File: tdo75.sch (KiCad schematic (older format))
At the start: 15 parts

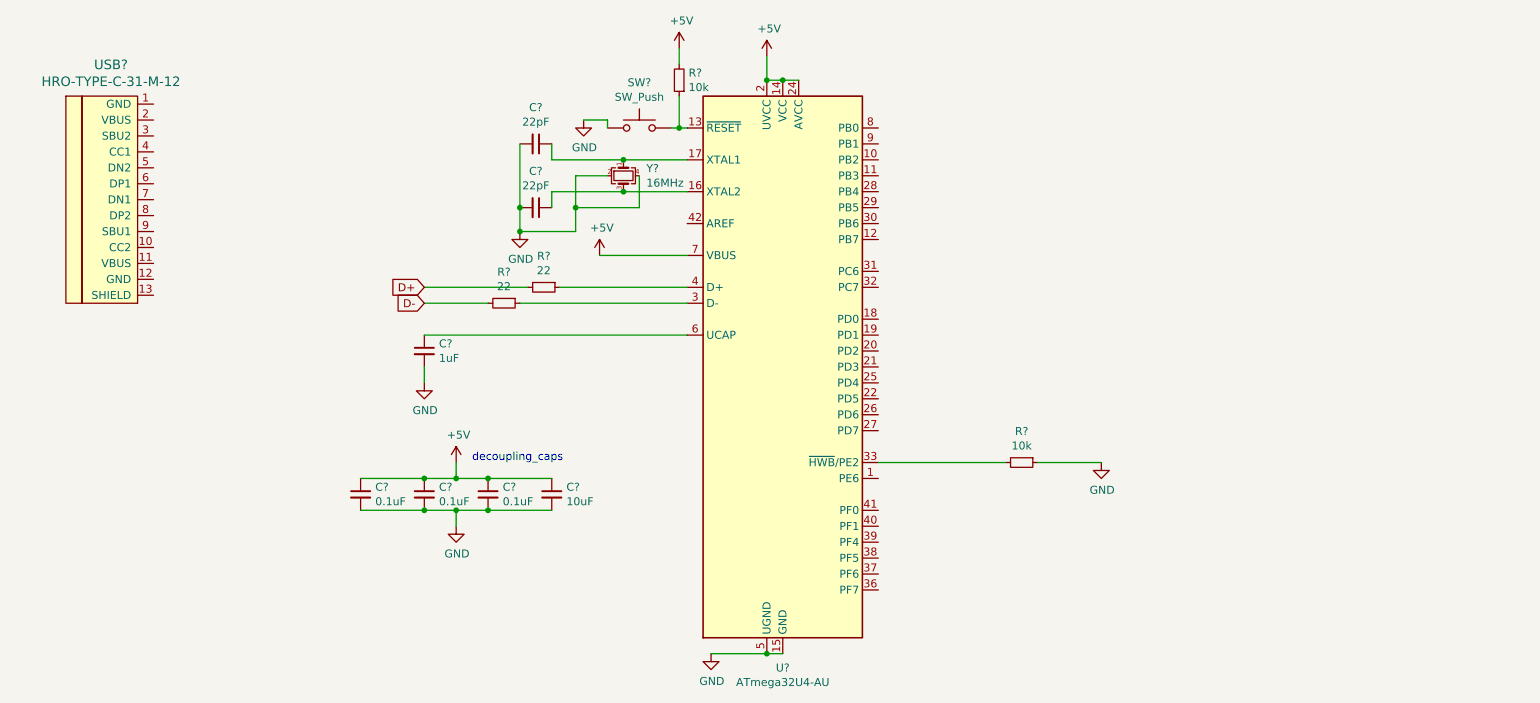
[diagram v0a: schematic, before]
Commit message: map footprints to schematics
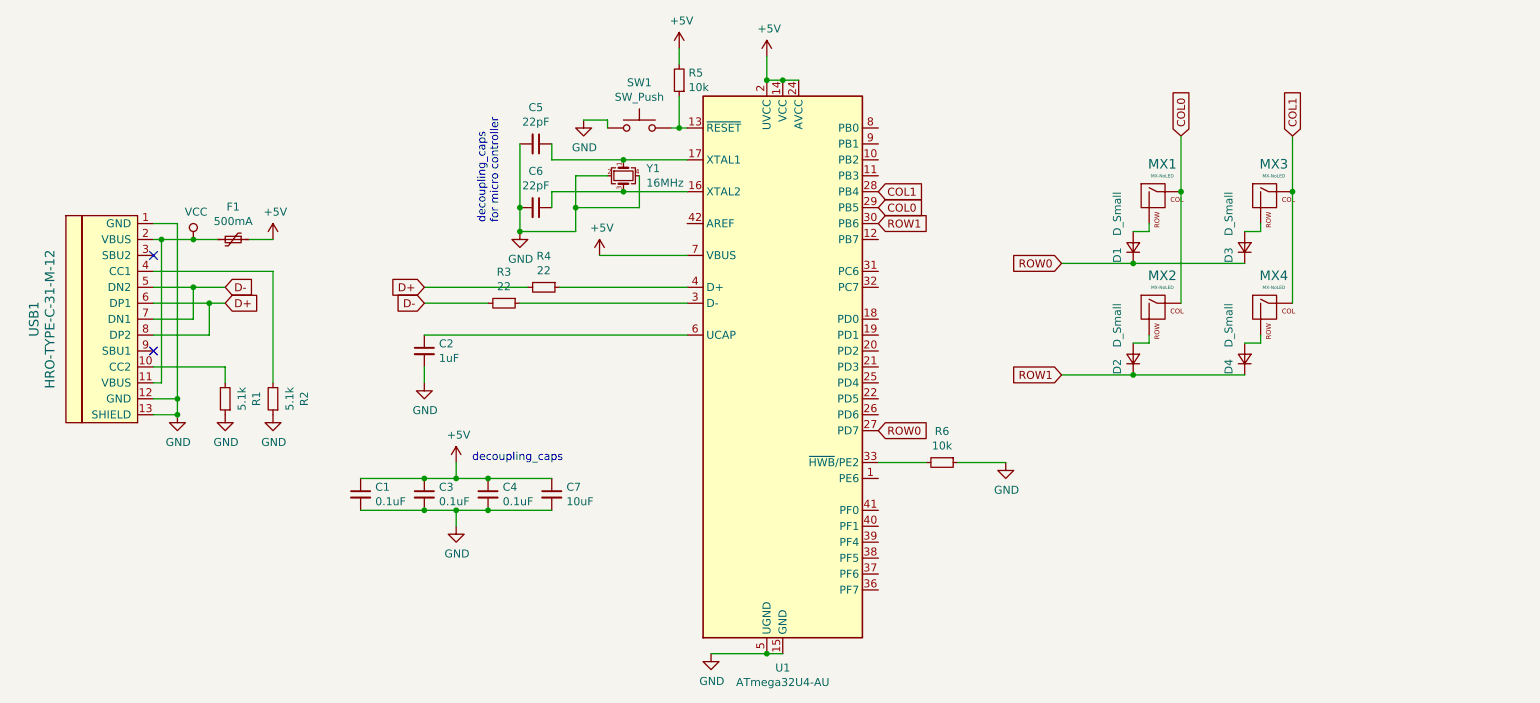
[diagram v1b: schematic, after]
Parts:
- added D1, D2, D3, D4: D_Small, Diode_SMD:D_SOD-123, symbol Device:D_Small
- added F1: 500mA, Fuse:Fuse_1206_3216Metric, symbol Device:Polyfuse_Small
- added MX1, MX2, MX3, MX4: MX-NoLED, MX_Only:MXOnly-1U-NoLED, symbol MX_Alps_Hybrid:MX-NoLED
- added R1, R2: 5.1k, Resistor_SMD:R_0805_2012Metric, symbol Device:R_Small
- C1, C2, C3, C4, C5, C6, C7: renamed from C?; footprint (none) -> Capacitor_SMD:C_0805_2012Metric
- R3, R4, R5, R6: renamed from R?; footprint (none) -> Resistor_SMD:R_0805_2012Metric
- SW1: renamed from SW?; footprint (none) -> random-keyboard-parts:SKQG-1155865
- USB1: renamed from USB?; footprint (none) -> Type-C:HRO-TYPE-C-31-M-12
- Y1: renamed from Y?; footprint (none) -> Crystal:Crystal_SMD_3225-4Pin_3.2x2.5mm
- gave numbers to parts that had none: 1
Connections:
- net +5V: now also F1.1
- net D+: now also USB1.6 (DP1), USB1.8 (DP2)
- net D-: now also USB1.5 (DN2), USB1.7 (DN1)
- net GND: now also USB1.1 (GND), USB1.12 (GND), USB1.13 (SHIELD), R1.1, R2.1
- net ROW0: now reaches U1.27 (PD7)
- net ROW0: now also D1.1 (K), D3.1 (K)
- net COL1: now reaches U1.28 (PB4)
- net COL1: now also MX3.1 (COL), MX4.1 (COL)
- net COL0: now reaches U1.29 (PB5)
- net COL0: now also MX1.1 (COL), MX2.1 (COL)
- net ROW1: now reaches U1.30 (PB6)
- net ROW1: now also D2.1 (K), D4.1 (K)
- net at USB1.10 (CC2): now also R1.2
- net VCC: now reaches USB1.11 (VBUS)
- net VCC: now also USB1.2 (VBUS), F1.2
- net at USB1.4 (CC1): now also R2.2
- new net: D1.2 (A), MX1.2 (ROW)
- new net: D2.2 (A), MX2.2 (ROW)
- new net: D4.2 (A), MX4.2 (ROW)
- new net: D3.2 (A), MX3.2 (ROW)
- no-connect marks 0 -> 2
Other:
- note added: "decoupling_caps \nfor micro controller\n\n"
- moved on the sheet: R6, USB1

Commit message: heirarchical keyboard matrix
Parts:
- removed D1, D2, D3, D4: D_Small, Diode_SMD:D_SOD-123, symbol Device:D_Small
- removed MX1, MX2, MX3, MX4: MX-NoLED, MX_Only:MXOnly-1U-NoLED, symbol MX_Alps_Hybrid:MX-NoLED
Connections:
- net COL0: now also U1.8 (PB0); no longer U1.29 (PB5)
- net COL1: now also U1.9 (PB1); no longer U1.28 (PB4)
- net ROW0: now also U1.41 (PF0); no longer U1.27 (PD7)
- net ROW1: now also U1.40 (PF1); no longer U1.30 (PB6)
- net COL2: now reaches U1.10 (PB2)
- net COL3: now reaches U1.11 (PB3)
- net COL7: now reaches U1.12 (PB7)
- net COL8: now reaches U1.18 (PD0)
- net COL9: now reaches U1.19 (PD1)
- net COL10: now reaches U1.20 (PD2)
- net COL11: now reaches U1.21 (PD3)
- net COL13: now reaches U1.22 (PD5)
- net COL12: now reaches U1.25 (PD4)
- net COL14: now reaches U1.26 (PD6)
- net ROW4: now reaches U1.37 (PF6)
- net ROW3: now reaches U1.38 (PF5)
- net ROW2: now reaches U1.39 (PF4)
- new net COL15: U1.27 (PD7)
- new net COL4: U1.28 (PB4)
- new net COL5: U1.29 (PB5)
- new net COL6: U1.30 (PB6)
- no-connect marks 2 -> 6
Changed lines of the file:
@@
 $Descr A4 11693 8268
 encoding utf-8
-Sheet 1 1
+Sheet 1 2
 Title ""
 Date ""
@@
 NoConn ~ 1550 4100
 NoConn ~ 1550 3500
-$Comp
-L MX_Alps_Hybrid:MX-NoLED MX1
-U 1 1 5E7B02A9
-P 7850 3150
-F 0 "MX1" H 7883 3373 60  0000 C CNN
-F 1 "MX-NoLED" H 7883 3299 20  0000 C CNN
-F 2 "MX_Only:MXOnly-1U-NoLED" H 7225 3125 60  0001 C CNN
-F 3 "" H 7225 3125 60  0001 C CNN
-	1    7850 3150
-	1    0    0    -1
-$EndComp
-$Comp
-L MX_Alps_Hybrid:MX-NoLED MX2
-U 1 1 5E7B0859
-P 7850 3850
-F 0 "MX2" H 7883 4073 60  0000 C CNN
-F 1 "MX-NoLED" H 7883 3999 20  0000 C CNN
-F 2 "MX_Only:MXOnly-1U-NoLED" H 7225 3825 60  0001 C CNN
-F 3 "" H 7225 3825 60  0001 C CNN
-	1    7850 3850
-	1    0    0    -1
-$EndComp
-$Comp
-L MX_Alps_Hybrid:MX-NoLED MX4
-U 1 1 5E7B0B55
-P 8550 3850
-F 0 "MX4" H 8583 4073 60  0000 C CNN
-F 1 "MX-NoLED" H 8583 3999 20  0000 C CNN
-F 2 "MX_Only:MXOnly-1U-NoLED" H 7925 3825 60  0001 C CNN
-F 3 "" H 7925 3825 60  0001 C CNN
-	1    8550 3850
-	1    0    0    -1
-$EndComp
-$Comp
-L MX_Alps_Hybrid:MX-NoLED MX3
-U 1 1 5E7B0E66
-P 8550 3150
-F 0 "MX3" H 8583 3373 60  0000 C CNN
-F 1 "MX-NoLED" H 8583 3299 20  0000 C CNN
-F 2 "MX_Only:MXOnly-1U-NoLED" H 7925 3125 60  0001 C CNN
-F 3 "" H 7925 3125 60  0001 C CNN
-	1    8550 3150
-	1    0    0    -1
-$EndComp
-$Comp
-L Device:D_Small D1
-U 1 1 5E7B3897
-P 7700 3450
-F 0 "D1" H 7700 3550 50  0000 R CNN
-F 1 "D_Small" H 8050 3550 50  0000 R CNN
-F 2 "Diode_SMD:D_SOD-123" V 7700 3450 50  0001 C CNN
-F 3 "~" V 7700 3450 50  0001 C CNN
-	1    7700 3450
-	0    -1   -1   0
-$EndComp
-Wire Wire Line
-	7700 3350 7800 3350
-Wire Wire Line
-	7800 3350 7800 3300
-$Comp
-L Device:D_Small D2
-U 1 1 5E7B58A6
-P 7700 4150
-F 0 "D2" H 7700 4250 50  0000 R CNN
-F 1 "D_Small" H 8050 4250 50  0000 R CNN
-F 2 "Diode_SMD:D_SOD-123" V 7700 4150 50  0001 C CNN
-F 3 "~" V 7700 4150 50  0001 C CNN
-	1    7700 4150
-	0    -1   -1   0
-$EndComp
-$Comp
-L Device:D_Small D4
-U 1 1 5E7B5B76
-P 8400 4150
-F 0 "D4" H 8400 4250 50  0000 R CNN
-F 1 "D_Small" H 8750 4250 50  0000 R CNN
-F 2 "Diode_SMD:D_SOD-123" V 8400 4150 50  0001 C CNN
-F 3 "~" V 8400 4150 50  0001 C CNN
-	1    8400 4150
-	0    -1   -1   0
-$EndComp
-$Comp
-L Device:D_Small D3
-U 1 1 5E7B5E2E
-P 8400 3450
-F 0 "D3" H 8400 3550 50  0000 R CNN
-F 1 "D_Small" H 8750 3550 50  0000 R CNN
-F 2 "Diode_SMD:D_SOD-123" V 8400 3450 50  0001 C CNN
-F 3 "~" V 8400 3450 50  0001 C CNN
-	1    8400 3450
-	0    -1   -1   0
-$EndComp
-Wire Wire Line
-	7700 4050 7800 4050
-Wire Wire Line
-	7800 4050 7800 4000
-Wire Wire Line
-	8400 4050 8500 4050
-Wire Wire Line
-	8500 4050 8500 4000
-Wire Wire Line
-	8400 3350 8500 3350
-Wire Wire Line
-	8500 3350 8500 3300
-Wire Wire Line
-	8000 3800 8000 3100
-Wire Wire Line
-	8000 3100 8000 2750
-Connection ~ 8000 3100
-Wire Wire Line
-	8400 3550 7700 3550
-Wire Wire Line
-	7700 3550 7250 3550
-Connection ~ 7700 3550
-Wire Wire Line
-	8400 4250 7700 4250
-Wire Wire Line
-	7700 4250 7250 4250
-Connection ~ 7700 4250
-Wire Wire Line
-	8700 3800 8700 3100
-Wire Wire Line
-	8700 3100 8700 2750
-Connection ~ 8700 3100
-Text GLabel 8000 2750 1    50   Input ~ 0
+Text GLabel 6100 2800 2    50   Input ~ 0
+COL1
+Text GLabel 6100 2700 2    50   Input ~ 0
 COL0
-Text GLabel 8700 2750 1    50   Input ~ 0
-COL1
-Text GLabel 7250 4250 0    50   Input ~ 0
-ROW1
-Text GLabel 7250 3550 0    50   Input ~ 0
+Text GLabel 6100 5100 2    50   Input ~ 0
 ROW0
-Text GLabel 6100 3100 2    50   Input ~ 0
-COL1
-Text GLabel 6100 3200 2    50   Input ~ 0
-COL0
-Text GLabel 6100 4600 2    50   Input ~ 0
-ROW0
-Text GLabel 6100 3300 2    50   Input ~ 0
+Text GLabel 6100 5200 2    50   Input ~ 0
 ROW1
 Wire Wire Line
@@
 Wire Wire Line
 	2150 3400 2300 3400
+$Sheet
+S 8600 2450 1550 600
+U 5E80119E
+F0 "KeyboardSwitchMatrix" 50
+F1 "keyboard-switch-matrix.sch" 50
+$EndSheet
+Text GLabel 6100 2900 2    50   Input ~ 0
+COL2
+Text GLabel 6100 3000 2    50   Input ~ 0
+COL3
+Text GLabel 6100 3100 2    50   Input ~ 0
+COL4
+Text GLabel 6100 3200 2    50   Input ~ 0
+COL5
+Text GLabel 6100 3300 2    50   Input ~ 0
+COL6
+Text GLabel 6100 3400 2    50   Input ~ 0
+COL7
+Text GLabel 6100 3900 2    50   Input ~ 0
+COL8
+Text GLabel 6100 4000 2    50   Input ~ 0
+COL9
+Text GLabel 6100 4100 2    50   Input ~ 0
+COL10
+Text GLabel 6100 4200 2    50   Input ~ 0
+COL11
+Text GLabel 6100 4300 2    50   Input ~ 0
+COL12
+Text GLabel 6100 4400 2    50   Input ~ 0
+COL13
+Text GLabel 6100 4500 2    50   Input ~ 0
+COL14
+Text GLabel 6100 4600 2    50   Input ~ 0
+COL15
+Text GLabel 6100 5300 2    50   Input ~ 0
+ROW2
+Text GLabel 6100 5400 2    50   Input ~ 0
+ROW3
+Text GLabel 6100 5500 2    50   Input ~ 0
+ROW4
+NoConn ~ 6100 5600
+NoConn ~ 6100 4900
+NoConn ~ 6100 3600
+NoConn ~ 6100 3700
 $EndSCHEMATC
